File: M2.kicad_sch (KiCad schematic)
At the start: 26 parts, among them J30 SM3ZS067U310ABR1200, J31 G85D1171012HHR, U13 RCLAMP0504PATCT, U33 MAX20074

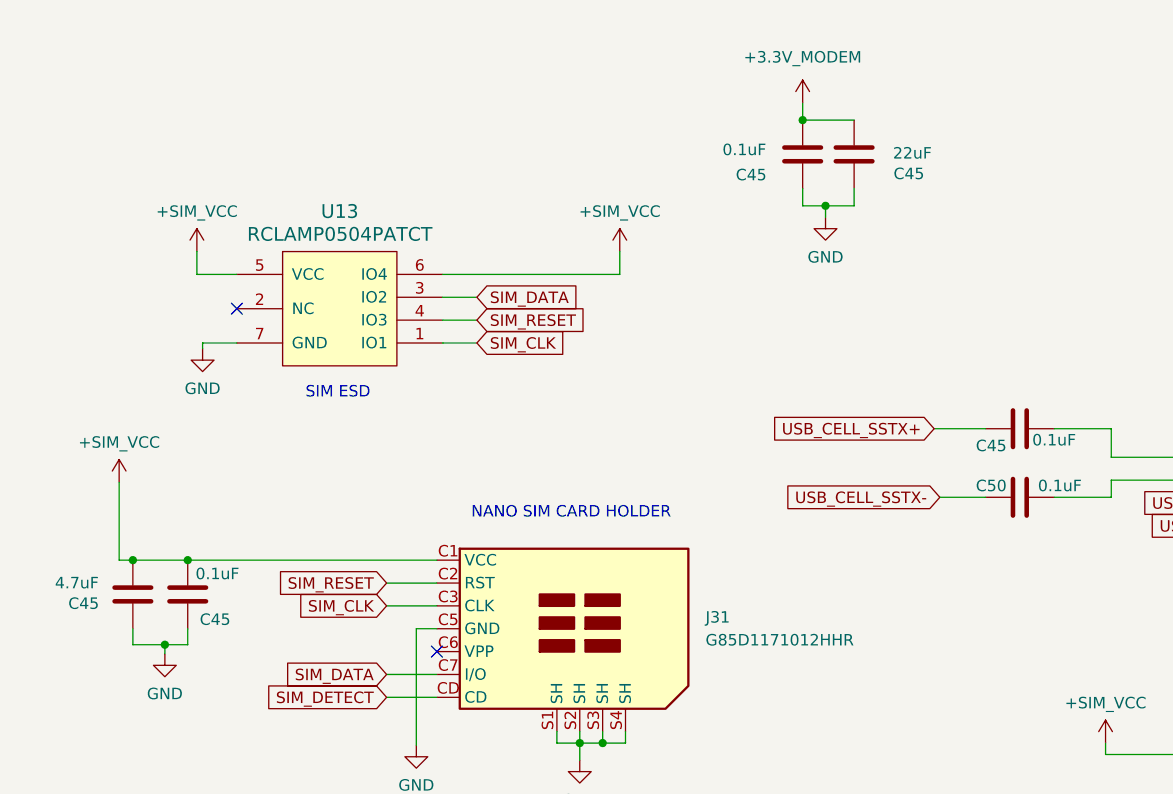
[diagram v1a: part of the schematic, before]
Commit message: updates for Rev1B boards, pinout changes on J5 and J8
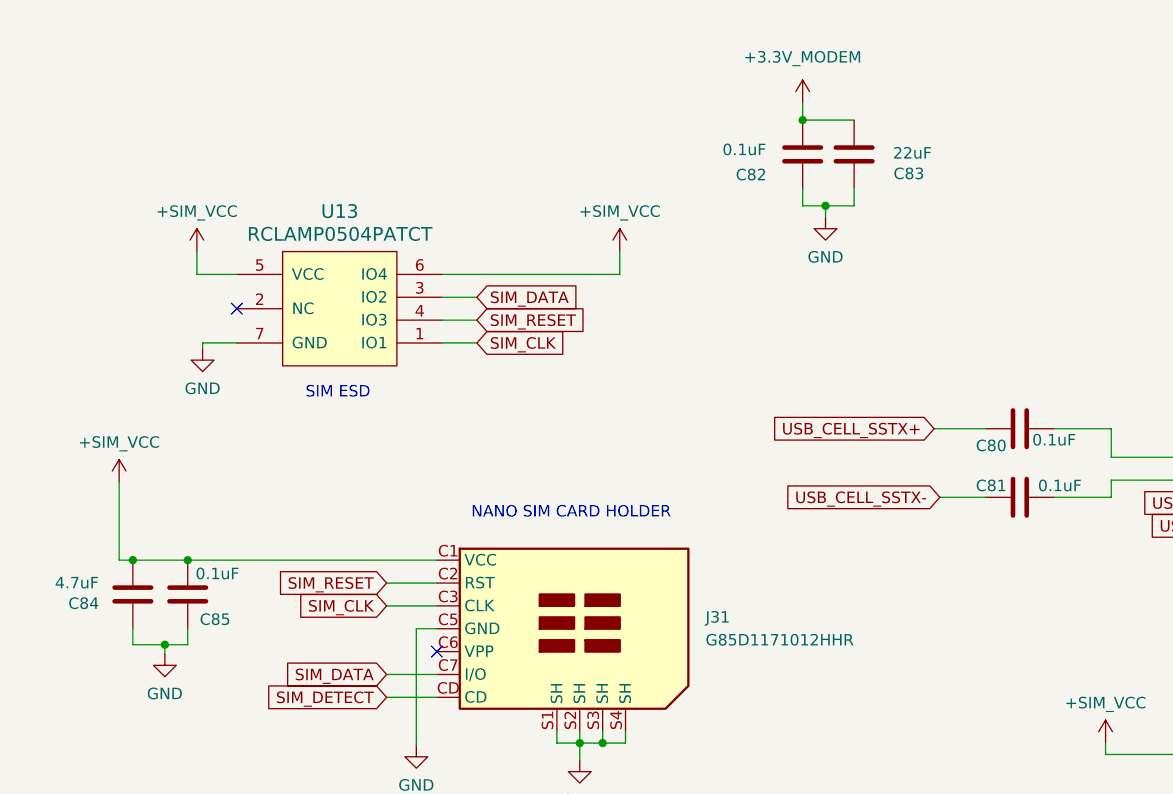
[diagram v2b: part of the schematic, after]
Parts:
- renumbered C45 to C80, C50 to C81, C45 to C82, C45 to C83, C45 to C84, C45 to C85
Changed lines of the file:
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@@
   (title_block
     (title "EchoPilot Carrier")
-    (rev "1")
+    (date "2023-10-25")
+    (rev "1B")
     (company "Echo MAV, LLC")
   )
@@
   (symbol (lib_id "archangel:+5V_FMU") (at 27.305 158.115 0) (unit 1)
     (in_bom yes) (on_board yes) (dnp no)
-    (property "Reference" "#PWR0111" (at 27.305 161.925 0)
+    (property "Reference" "#PWR0234" (at 27.305 161.925 0)
       (effects (font (size 1.27 1.27)) hide)
     )
@@
     (instances
       (project "echopilot_ai_carrier"
-        (path "/c1cd829b-ce6d-45d4-ac65-d2dab15a61f6/00000000-0000-0000-0000-0000637b8aa2"
-          (reference "#PWR0111") (unit 1)
-        )
         (path "/c1cd829b-ce6d-45d4-ac65-d2dab15a61f6/9fdd2f6a-b8c4-42a4-8efd-592d9522450d"
           (reference "#PWR0234") (unit 1)
@@
   (symbol (lib_id "archangel:+5V_FMU") (at 48.895 125.095 0) (unit 1)
     (in_bom yes) (on_board yes) (dnp no)
-    (property "Reference" "#PWR0111" (at 48.895 128.905 0)
+    (property "Reference" "#PWR0220" (at 48.895 128.905 0)
       (effects (font (size 1.27 1.27)) hide)
     )
@@
     (instances
       (project "echopilot_ai_carrier"
-        (path "/c1cd829b-ce6d-45d4-ac65-d2dab15a61f6/00000000-0000-0000-0000-0000637b8aa2"
-          (reference "#PWR0111") (unit 1)
-        )
         (path "/c1cd829b-ce6d-45d4-ac65-d2dab15a61f6/9fdd2f6a-b8c4-42a4-8efd-592d9522450d"
           (reference "#PWR0220") (unit 1)
@@
   (symbol (lib_id "Device:C") (at 133.985 68.58 90) (unit 1)
     (in_bom yes) (on_board yes) (dnp no)
-    (property "Reference" "C50" (at 130.81 67.31 90)
+    (property "Reference" "C81" (at 130.81 67.31 90)
       (effects (font (size 1.27 1.27)))
     )
@@
     (instances
       (project "echopilot_ai_carrier"
-        (path "/c1cd829b-ce6d-45d4-ac65-d2dab15a61f6/1d1bbc38-a8f2-4a8f-9261-c0513d875619"
-          (reference "C50") (unit 1)
-        )
         (path "/c1cd829b-ce6d-45d4-ac65-d2dab15a61f6/9fdd2f6a-b8c4-42a4-8efd-592d9522450d"
           (reference "C81") (unit 1)
@@
   (symbol (lib_id "Device:C") (at 115.57 30.48 180) (unit 1)
     (in_bom yes) (on_board yes) (dnp no)
-    (property "Reference" "C45" (at 121.666 32.639 0)
+    (property "Reference" "C83" (at 121.666 32.639 0)
       (effects (font (size 1.27 1.27)))
     )
@@
     (instances
       (project "echopilot_ai_carrier"
-        (path "/c1cd829b-ce6d-45d4-ac65-d2dab15a61f6/1d1bbc38-a8f2-4a8f-9261-c0513d875619"
-          (reference "C45") (unit 1)
-        )
         (path "/c1cd829b-ce6d-45d4-ac65-d2dab15a61f6/9fdd2f6a-b8c4-42a4-8efd-592d9522450d"
           (reference "C83") (unit 1)
@@
   (symbol (lib_id "Device:C") (at 35.433 79.375 180) (unit 1)
     (in_bom yes) (on_board yes) (dnp no)
-    (property "Reference" "C45" (at 29.972 80.391 0)
+    (property "Reference" "C84" (at 29.972 80.391 0)
       (effects (font (size 1.27 1.27)))
     )
@@
     (instances
       (project "echopilot_ai_carrier"
-        (path "/c1cd829b-ce6d-45d4-ac65-d2dab15a61f6/1d1bbc38-a8f2-4a8f-9261-c0513d875619"
-          (reference "C45") (unit 1)
-        )
         (path "/c1cd829b-ce6d-45d4-ac65-d2dab15a61f6/9fdd2f6a-b8c4-42a4-8efd-592d9522450d"
           (reference "C84") (unit 1)
@@
   (symbol (lib_id "Device:C") (at 133.985 60.96 90) (unit 1)
     (in_bom yes) (on_board yes) (dnp no)
-    (property "Reference" "C45" (at 130.81 62.865 90)
+    (property "Reference" "C80" (at 130.81 62.865 90)
       (effects (font (size 1.27 1.27)))
     )
@@
     (instances
       (project "echopilot_ai_carrier"
-        (path "/c1cd829b-ce6d-45d4-ac65-d2dab15a61f6/1d1bbc38-a8f2-4a8f-9261-c0513d875619"
-          (reference "C45") (unit 1)
-        )
         (path "/c1cd829b-ce6d-45d4-ac65-d2dab15a61f6/9fdd2f6a-b8c4-42a4-8efd-592d9522450d"
           (reference "C80") (unit 1)
@@
   (symbol (lib_id "archangel:+5V_FMU") (at 93.345 166.37 0) (unit 1)
     (in_bom yes) (on_board yes) (dnp no)
-    (property "Reference" "#PWR0111" (at 93.345 170.18 0)
+    (property "Reference" "#PWR0152" (at 93.345 170.18 0)
       (effects (font (size 1.27 1.27)) hide)
     )
@@
     (instances
       (project "echopilot_ai_carrier"
-        (path "/c1cd829b-ce6d-45d4-ac65-d2dab15a61f6/00000000-0000-0000-0000-0000637b8aa2"
-          (reference "#PWR0111") (unit 1)
-        )
         (path "/c1cd829b-ce6d-45d4-ac65-d2dab15a61f6/9fdd2f6a-b8c4-42a4-8efd-592d9522450d"
           (reference "#PWR0152") (unit 1)
@@
   (symbol (lib_id "Device:C") (at 41.529 79.375 180) (unit 1)
     (in_bom yes) (on_board yes) (dnp no)
-    (property "Reference" "C45" (at 44.577 82.169 0)
+    (property "Reference" "C85" (at 44.577 82.169 0)
       (effects (font (size 1.27 1.27)))
     )
@@
     (instances
       (project "echopilot_ai_carrier"
-        (path "/c1cd829b-ce6d-45d4-ac65-d2dab15a61f6/1d1bbc38-a8f2-4a8f-9261-c0513d875619"
-          (reference "C45") (unit 1)
-        )
         (path "/c1cd829b-ce6d-45d4-ac65-d2dab15a61f6/9fdd2f6a-b8c4-42a4-8efd-592d9522450d"
           (reference "C85") (unit 1)
@@
   (symbol (lib_id "Device:C") (at 109.855 30.48 180) (unit 1)
     (in_bom yes) (on_board yes) (dnp no)
-    (property "Reference" "C45" (at 104.14 32.766 0)
+    (property "Reference" "C82" (at 104.14 32.766 0)
       (effects (font (size 1.27 1.27)))
     )
@@
     (instances
       (project "echopilot_ai_carrier"
-        (path "/c1cd829b-ce6d-45d4-ac65-d2dab15a61f6/1d1bbc38-a8f2-4a8f-9261-c0513d875619"
-          (reference "C45") (unit 1)
-        )
         (path "/c1cd829b-ce6d-45d4-ac65-d2dab15a61f6/9fdd2f6a-b8c4-42a4-8efd-592d9522450d"
           (reference "C82") (unit 1)
